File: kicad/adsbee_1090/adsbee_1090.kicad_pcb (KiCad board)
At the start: 4 copper layers, 33.5 x 30 mm, 72 parts, among them J1 U.FL 6GHz 50R, J2 USB_Micro-B_Receptacle, J3 Conn_02x03_Odd_Even, J4 Conn_ARM_JTAG_SWD_10, SW1 SW_Push, SW2 SW_Push, U1 AD8314, U2 BGA2818, U3 MCP6566, U4 AP2112K-3.3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

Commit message: Get PWM partially working
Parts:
- Y1: footprint Crystal:Crystal_SMD_SeikoEpson_FA238-4Pin_3.2x2.5mm -> Crystal:Crystal_SMD_3225-4Pin_3.2x2.5mm

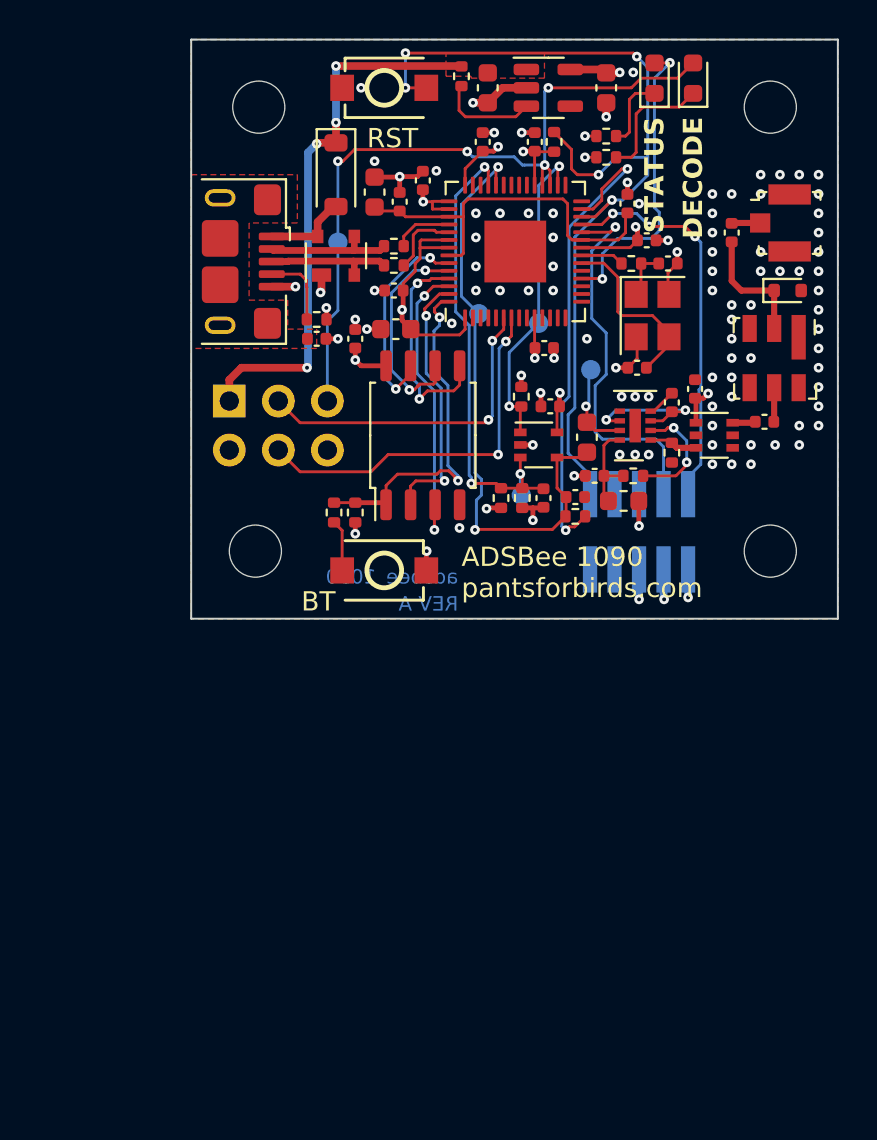
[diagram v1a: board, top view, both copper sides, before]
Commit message: Add hysteresis and begin work on Rev B PCB
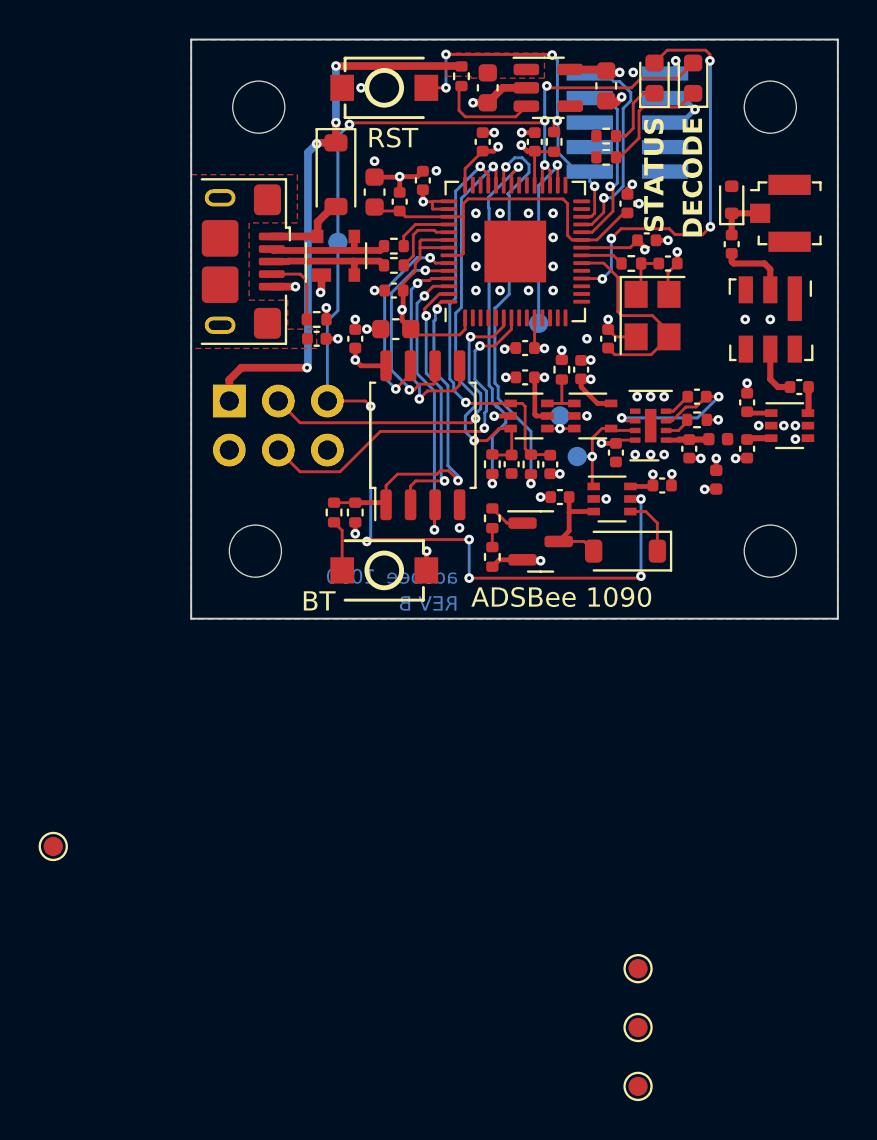
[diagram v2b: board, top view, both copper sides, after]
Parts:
- added C26: 7pF, Capacitor_SMD:C_0402_1005Metric, F.Cu at (63.8, 56.7)
- added C27: DNP, Capacitor_SMD:C_0402_1005Metric, F.Cu at (60.8, 56.7)
- added C28: 0.1uF, Capacitor_SMD:C_0402_1005Metric, F.Cu at (59.4, 58.6)
- added C29: 22nF, Capacitor_SMD:C_0402_1005Metric, F.Cu at (54.1, 59.2)
- added D5: 20V 1A, Diode_SMD:D_SOD-123, F.Cu at (57.5, 62.0)
- added L2: 12nH, Inductor_SMD:L_0402_1005Metric, F.Cu at (62.3, 56.2)
- added Q1: BSS84, Package_TO_SOT_SMD:SOT-23, F.Cu at (53.1, 61.5)
- added SW3: SN74LVC1G3157, Package_TO_SOT_SMD:SOT-363_SC-70-6, F.Cu at (52.5, 55.0)
- added TP6: TestPoint, TestPoint:TestPoint_Pad_D1.0mm, F.Cu at (58.1, 86.7)
- added TP7: TestPoint, TestPoint:TestPoint_Pad_D1.0mm, F.Cu at (58.1, 89.7)
- added TP8: TestPoint, TestPoint:TestPoint_Pad_D1.0mm, F.Cu at (27.9, 77.3)
- added U7: OPA358AIDCKR, Package_TO_SOT_SMD:SOT-363_SC-70-6, F.Cu at (56.8, 59.3)
- C21: value 2.2uF -> 1uF
- C7: value 1uF -> 0.1uF; footprint Capacitor_SMD:C_0603_1608Metric -> Capacitor_SMD:C_0402_1005Metric
- L1: footprint Inductor_SMD:L_0603_1608Metric -> Inductor_SMD:L_0402_1005Metric
- R2: value 4.99k -> 10k
- R5: value 52.3R -> 10k
- R6: value 10k -> 115R
- TP3: moved to F.Cu
- Y1: value 12.000MHz 18pF -> 12.000MHz 18pF ±20ppm 80R
- moved TP3 34.9 mm to (58.1, 83.6), turned to 0 degrees
- moved J4 21.2 mm to (57.6, 39.8), turned to 180 degrees
- moved GRAPHIC1 11.5 mm to (61.5, 50.3)
- moved R5 10.8 mm to (50.6, 62.3)
- moved D1 5.52 mm to (63.0, 43.8), turned to 90 degrees
- moved L1 4.92 mm to (62.2, 58.3), turned to -90 degrees
- moved TP1 4.56 mm to (54.1, 55.0)
- moved TP2 4.55 mm to (55.0, 57.1)
- moved C7 4.46 mm to (52.3, 53.0), turned to 180 degrees
- moved R3 4.40 mm to (61.2, 55.2), turned to 180 degrees
- moved R6 4.30 mm to (50.6, 60.3), turned to -90 degrees
- moved U2 3.93 mm to (66.0, 55.5)
- moved C9 3.71 mm to (51.6, 57.5), turned to -90 degrees
- moved U3 3.18 mm to (55.8, 55.0)
- moved C1 2.79 mm to (63.8, 54.3)
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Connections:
- net Net-(U1-VPOS) renamed /3V3_FILT_RF_DET
- C2 pad 1: /COMP_REF -> /MTL_HI_BIAS
- C7 pad 1: /RF_DET_OUT -> +3V3
- C7 pad 2: /COMP_BIAS_DC -> GND
- C9 pad 1: /COMP_BIAS_DC -> /MTL_LO_BIAS
- D1 pad 1: /RF_SAW_IN -> /RF_IN
- R1 pad 1: +3V3 -> /MTL_HI_BIAS
- R1 pad 2: /COMP_REF -> /MTL_HI_PWM
- R2 pad 1: /COMP_REF -> /MTL_LO_BIAS
- R2 pad 2: GND -> /MTL_LO_PWM
- R5 pad 1: /RF_DET_IN -> /~{RSSI_CLEAR}
- R5 pad 2: GND -> +3V3
- R6 pad 1: /COMP_BIAS_PWM -> Net-(Q1-G)
- R6 pad 2: /COMP_BIAS_DC -> /~{RSSI_CLEAR}
- TP1 pad 1: /COMP_REF -> /MTL_BIAS
- TP3 pad 1: /COMP_BIAS_DC -> /MTL_LO_BIAS
- U1 pad 1: /RF_DET_IN -> /RF_DET_IN_MATCHED
- U3 pad 3: /COMP_REF -> /MTL_BIAS
- U3 pad 4: /COMP_BIAS_DC -> /RF_DET_OUT
- U6 pad 27: /COMP_BIAS_PWM -> unconnected-(U6-GPIO16-Pad27)
- U6 pad 34: unconnected-(U6-GPIO22-Pad34) -> /RECOVERED_CLK
- U6 pad 36: unconnected-(U6-GPIO24-Pad36) -> /MTL_LO_PWM
- U6 pad 37: unconnected-(U6-GPIO25-Pad37) -> /MTL_HI_PWM
- U6 pad 38: /COMP_BIAS_DC -> /MTL_LO_BIAS
- U6 pad 39: /COMP_REF -> /MTL_HI_BIAS
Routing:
- net /DECODE: track 38.3 -> 69.8 mm, vias 4 -> 10
- net /COMP_BIAS_DC: track 31.0 -> 0.00 mm, vias 2 -> 0
- net /~{RESET}: track 49.0 -> 19.2 mm
- net /COMP_BIAS_PWM: track 25.1 -> 0.00 mm, vias 2 -> 0
- net /COMP_REF: track 25.0 -> 0.00 mm, vias 3 -> 0
- net /MTL_LO_BIAS: track 0.00 -> 21.4 mm, vias 0 -> 2
- net /MTL_HI_BIAS: track 0.00 -> 21.2 mm, vias 0 -> 2
- net /MTL_HI_PWM: track 0.00 -> 21.1 mm, vias 0 -> 2
- net /MTL_LO_PWM: track 0.00 -> 19.3 mm, vias 0 -> 2
- net Net-(J4-SWDCLK/TCK): track 19.9 -> 9.35 mm
- net Net-(J4-SWDIO/TMS): track 20.4 -> 11.0 mm, vias 3 -> 1
- net +3V3: track 41.2 -> 47.6 mm, vias 15 -> 17
- net /RSSI_HOLD: track 0.00 -> 5.84 mm
- net /STATUS_LED: track 15.8 -> 21.2 mm, vias 2 -> 4
- net Net-(U1-ENBL): track 5.95 -> 1.28 mm, vias 2 -> 0
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- added copper zone on In2.Cu, net /3V3_FILT_RF_DET
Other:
- board text added: "ADSBee 1090"
- board text removed: "ADSBee 1090 pantsforbirds.com"

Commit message: Make Rev B PCB
* Add dual references for MTL hysteresis.
* Add RSSI capture circuit.
* Remove large raw files from LTSpice folder.
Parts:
- TP3, TP6, TP7, TP8: moved to B.Cu
- moved TP7 50.2 mm to (51.1, 40.0), turned to 180 degrees
- moved TP3 35.0 mm to (49.7, 49.7), turned to 180 degrees
- moved TP8 31.2 mm to (54.6, 61.3), turned to 180 degrees
- moved TP6 30.7 mm to (49.2, 57.3), turned to 180 degrees
- moved TP4 3.70 mm to (53.0, 46.5)
- moved C13 1.50 mm to (48.6, 40.8), turned to 0 degrees
- moved TP2 1.36 mm to (55.4, 58.4)
- moved TP1 0.73 mm to (53.4, 54.8)
- moved C3 0.51 mm to (56.5, 57.0), turned to 0 degrees
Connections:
- U6 pad 11: unconnected-(U6-GPIO8-Pad11) -> /~{RSSI_CLEAR}
- U6 pad 40: unconnected-(U6-GPIO28_ADC2-Pad40) -> /RSSI_HOLD
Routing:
- net /RSSI_HOLD: track 5.84 -> 35.2 mm, vias 0 -> 4
- net /~{RSSI_CLEAR}: track 0.98 -> 15.1 mm, vias 0 -> 2
- net /MTL_HI_BIAS: track 21.2 -> 27.6 mm
- net /PULSES: track 12.3 -> 16.4 mm, vias 1 -> 2
- net /RECOVERED_CLK: track 0.00 -> 3.74 mm, vias 0 -> 1
- net /MTL_HI_PWM: track 21.1 -> 19.1 mm
- net +3V3: track 47.6 -> 48.8 mm, vias 17 -> 18
- net /MTL_LO_PWM: track 19.3 -> 20.5 mm
- net /MTL_LO_BIAS: track 21.4 -> 22.5 mm
- net /RF_DET_IN: track 1.42 -> 2.44 mm
- net /UART_RX: track 19.3 -> 18.3 mm
- net /RF_DET_VSET: track 9.49 -> 10.3 mm
- net /QSPI_SCLK: track 11.4 -> 10.8 mm
- net GND: track 29.6 -> 29.7 mm, vias 60 -> 61
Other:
- board text added: "MTL_BIAS"
- board text added: "MTL_HI_BIAS"
- board text added: "MTL_LO_BIAS"
- board text added: "RECOVERED_CLK"
- board text added: "RSSI_HOLD"
- board text added: "SWDCLK"
- board text added: "~{RESET}"
- board text removed: "COMP_BIAS_DC"
- board text removed: "COMP_REF"
- board text removed: "SWCLK"
